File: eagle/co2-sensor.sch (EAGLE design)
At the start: 12 parts, among them IC1 LM1117IMPX-3.3, J1 MH-Z19, U1 esp12e, U2 dht22, X1 usb

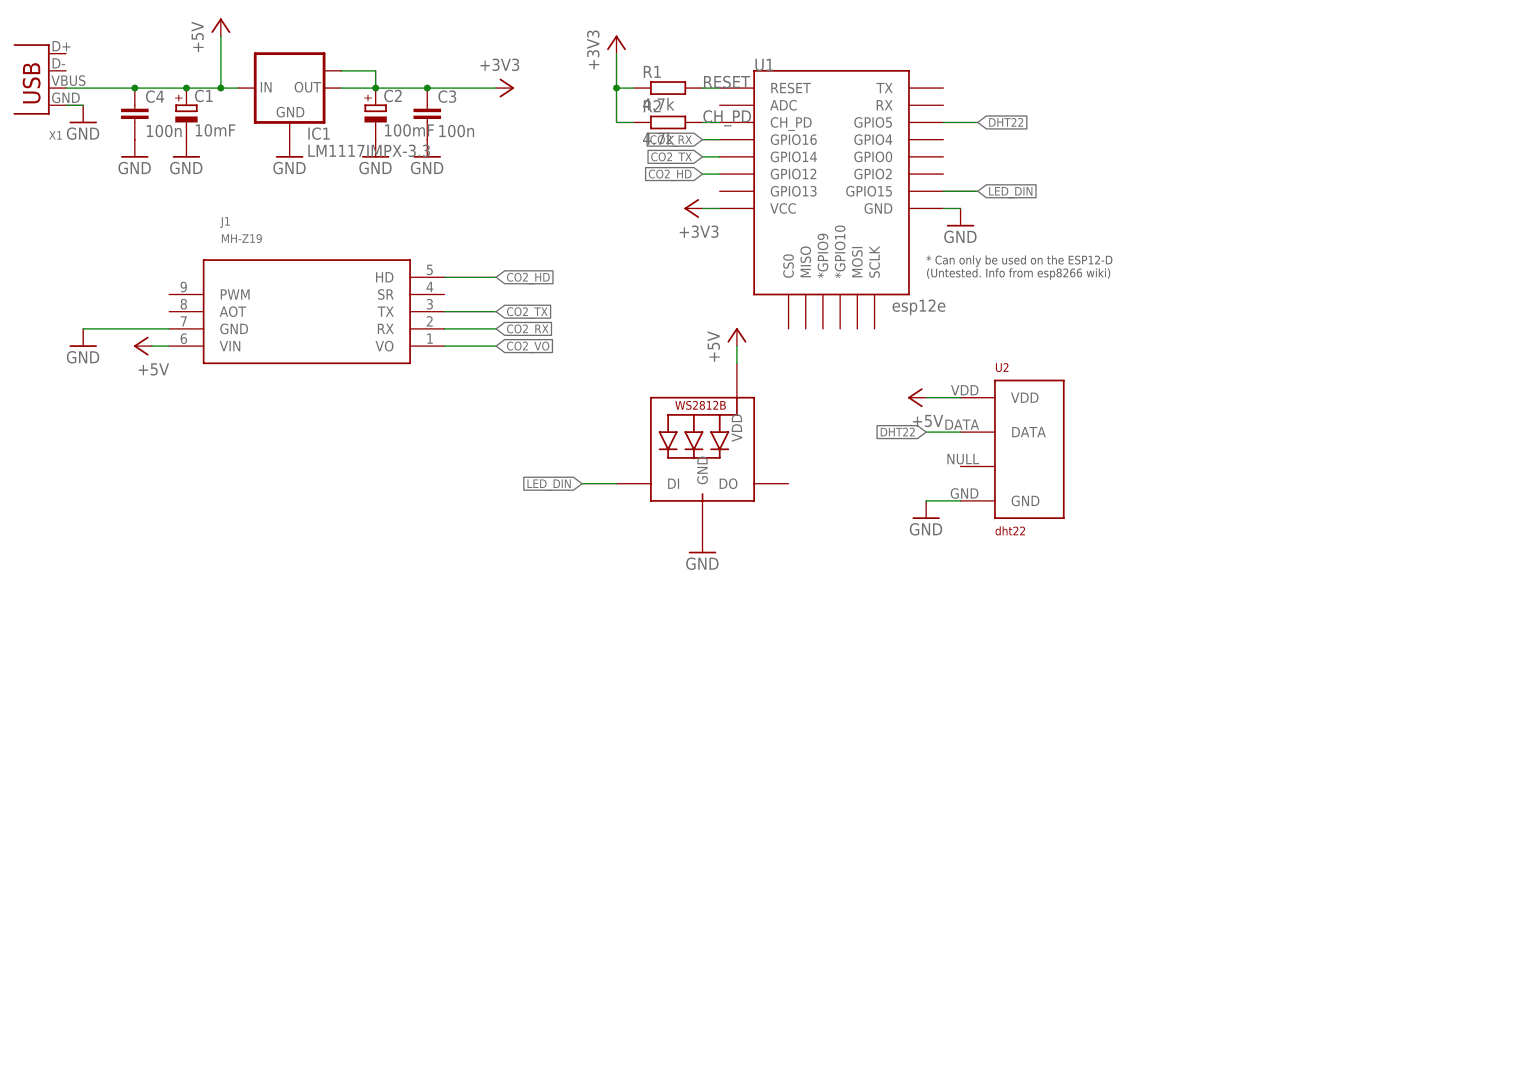
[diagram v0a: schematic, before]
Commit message: fixed prototype issues
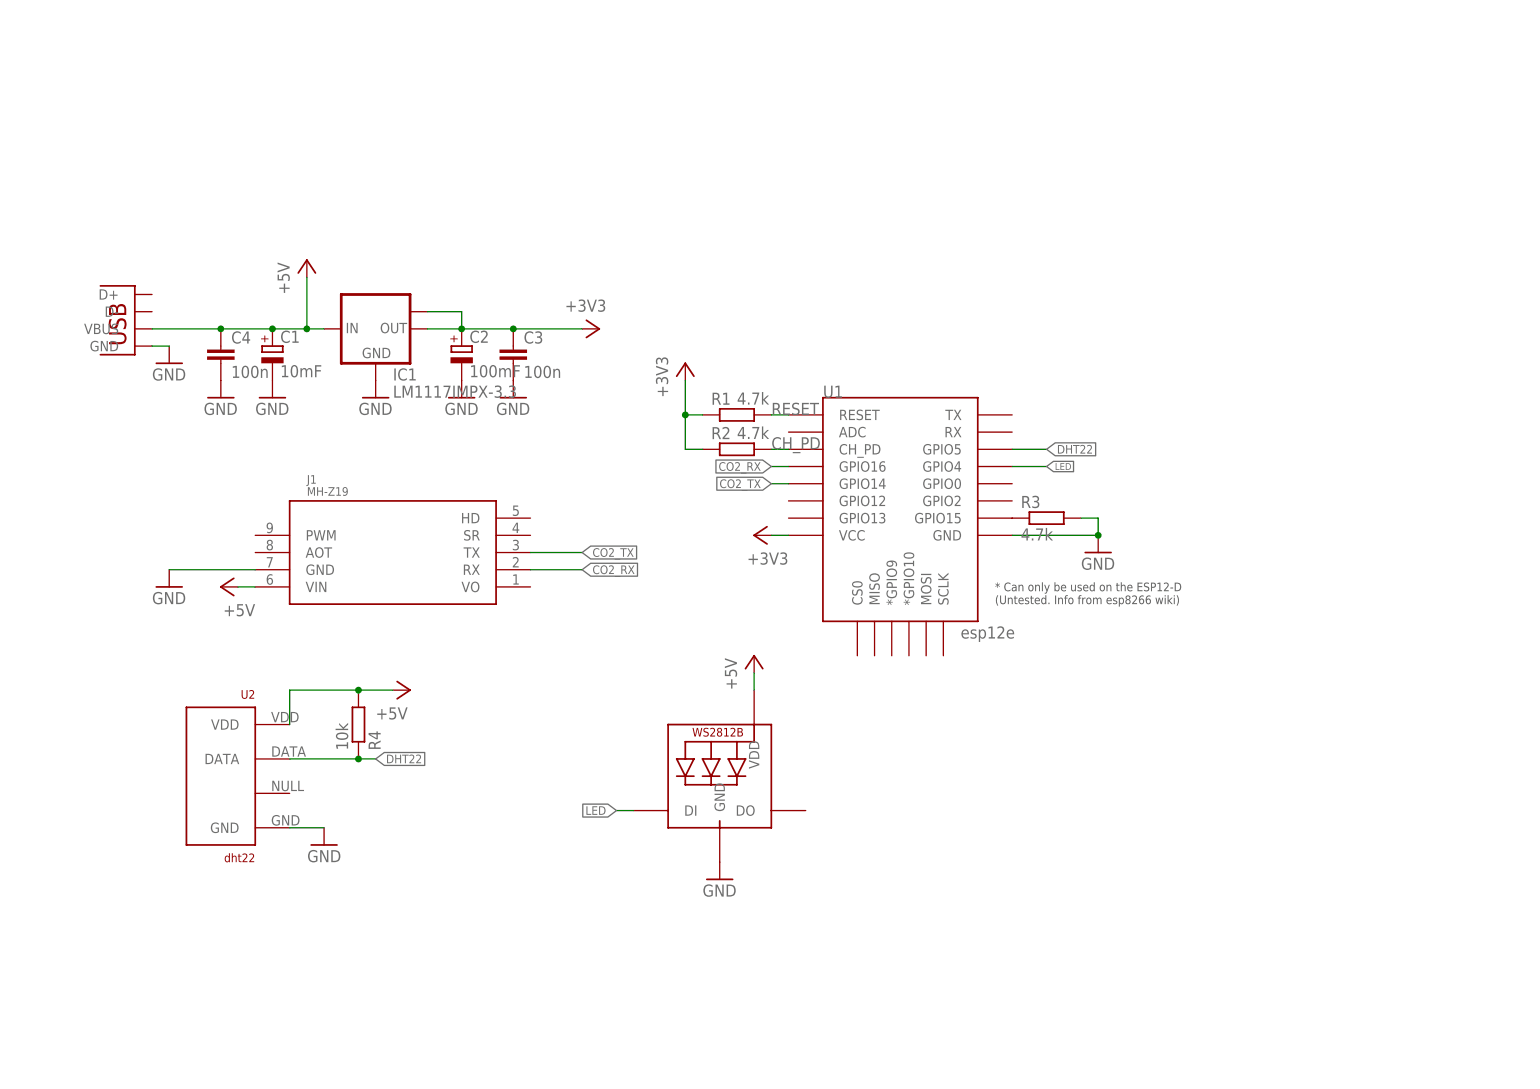
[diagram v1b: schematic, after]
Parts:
- removed X1: usb, con-usb-3:USB-A-H
- added R3: 4.7k, rcl:R-EU_M0805
- added R4: 10k, rcl:R-EU_M0805
- added U$1: USB-A, usb:USB-A
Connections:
- removed net CO2_HD: J1.HD, U1.GPIO12
- removed net CO2_VO: J1.VO
- removed net LED_DIN: LED1.DI, U1.GPIO15
- new net LED: LED1.DI, U1.GPIO4
- new net N$1: R3.1, U1.GPIO15
- net +5V: now also R4.2, U$1.VBUS; no longer X1.VBUS
- net DHT22: now also R4.1
- net GND: now also R3.2, U$1.GND@1; no longer X1.GND
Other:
- moved on the sheet: C1, C2, C3, C4, IC1, J1, R1, R2, U1, U2

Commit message: .
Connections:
- net GND: now also U$1.GND@2, U$1.GND@3
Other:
- moved on the sheet: R4

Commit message: .
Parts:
- removed C1: 10mF, rcl:CPOL-EUCT3216
- added BT1: BAT-HLD-012-SMT, BAT-HLD-012-SMT:BAT-HLD-012-SMT
- added IC2: (no value), DS3231_industrialberry:DS3231SOIC-16W
- added JP1: (no value), pinhead:PINHD-1X4
- added JP2: (no value), pinhead:PINHD-2X4
- added R5, R6: 4.7k, rcl:R-EU_M0805
- C4: value 100n -> 10u
- LED1: value WS2812B_5050N -> WS2812B5050; device WS2812B:WS2812B_5050N -> WS2812B:WS2812B5050
- U$1: value USB-A -> USB-C; device usb:USB-A -> USB-C:USB-C
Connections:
- removed net LED: LED1.DI, U1.GPIO4
- removed net RESET: R1.2, U1.RESET
- new net CLOCK_INT: IC2.!INT, U1.GPIO13
- new net IO0: JP2.5, U1.GPIO0
- new net IO2: JP2.3, LED1.DI, U1.GPIO2
- new net N$6: BT1.P, IC2.VBAT
- new net RST: IC2.!RST, JP2.6, R2.2, U1.RESET
- new net RXD: JP2.7, U1.RX
- new net SCL: IC2.SCL, JP1.3, R6.2, U1.GPIO5
- new net SDA: IC2.SDA, JP1.4, R5.2, U1.GPIO4
- new net TXD: JP2.2, U1.TX
- net +3V3: now also IC2.VCC, JP1.2, JP2.8, R5.1, R6.1
- net +5V: no longer C1.+
- net CH_PD: now also JP2.4, R1.2; no longer R2.2
- net DHT22: now also U1.GPIO12; no longer U1.GPIO5
- net GND: now also BT1.N, IC2.GND, IC2.NC@1, IC2.NC@2, IC2.NC@3, IC2.NC@4, IC2.NC@5, IC2.NC@6, IC2.NC@7, IC2.NC@8, JP1.1, JP2.1, U$1.GND; no longer C1.-, U$1.GND@1, U$1.GND@2, U$1.GND@3
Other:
- moved on the sheet: C4, R1, R2, R3, U1

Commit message: .
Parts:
- added C1: 100n, rcl:C-EUC0805
- added U3: BMP280, BMP280:BMP280
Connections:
- net +3V3: now also C1.1, U3.CSB, U3.VDD, U3.VDDIO
- net GND: now also C1.2, U3.GND, U3.SDO
- net SCL: now also U3.SCK
- net SDA: now also U3.SDI
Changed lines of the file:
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@@
 </variantdefs>
 <classes>
-<class number="0" name="default" width="0.2" drill="0">
+<class number="0" name="default" width="0.25" drill="0">
 <clearance class="0" value="0.205"/>
 </class>
-<class number="1" name="GND" width="1" drill="0">
+<class number="1" name="GND" width="0.8" drill="0">
 <clearance class="0" value="0.205"/>
 <clearance class="1" value="0.205"/>
 </class>
-<class number="2" name="+5V" width="0.8" drill="0">
+<class number="2" name="+5V" width="0.5" drill="0">
 <clearance class="0" value="0.205"/>
 <clearance class="1" value="0.205"/>
 <clearance class="2" value="0.205"/>
 </class>
-<class number="3" name="+3.3V" width="0.8" drill="0">
+<class number="3" name="+3.3V" width="0.5" drill="0">
 <clearance class="0" value="0.205"/>
 <clearance class="1" value="0.205"/>
@@
 <part name="GND12" library="supply1" library_urn="urn:adsk.eagle:library:371" deviceset="GND" device=""/>
 <part name="P+2" library="supply1" library_urn="urn:adsk.eagle:library:371" deviceset="+5V" device=""/>
+<part name="U3" library="BMP280" deviceset="BMP280" device=""/>
+<part name="GND13" library="supply1" library_urn="urn:adsk.eagle:library:371" deviceset="GND" device=""/>
+<part name="GND14" library="supply1" library_urn="urn:adsk.eagle:library:371" deviceset="GND" device=""/>
+<part name="+3V4" library="supply1" library_urn="urn:adsk.eagle:library:371" deviceset="+3V3" device=""/>
+<part name="C1" library="rcl" library_urn="urn:adsk.eagle:library:334" deviceset="C-EU" device="C0805" package3d_urn="urn:adsk.eagle:package:23617/2" value="100n"/>
+<part name="GND15" library="supply1" library_urn="urn:adsk.eagle:library:371" deviceset="GND" device=""/>
 </parts>
 <sheets>
@@
 <instance part="P+2" gate="1" x="187.96" y="-7.62" smashed="yes">
 <attribute name="VALUE" x="185.42" y="-12.7" size="1.778" layer="96" rot="R90"/>
+</instance>
+<instance part="U3" gate="G$1" x="35.56" y="-104.14" smashed="yes">
+<attribute name="NAME" x="25.3804" y="-96.50533125" size="1.78141875" layer="95"/>
+<attribute name="VALUE" x="25.3907" y="-114.3093" size="1.77963125" layer="96"/>
+</instance>
+<instance part="GND13" gate="1" x="48.26" y="-114.3" smashed="yes">
+<attribute name="VALUE" x="45.72" y="-116.84" size="1.778" layer="96"/>
+</instance>
+<instance part="GND14" gate="1" x="12.7" y="-114.3" smashed="yes">
+<attribute name="VALUE" x="10.16" y="-116.84" size="1.778" layer="96"/>
+</instance>
+<instance part="+3V4" gate="G$1" x="50.8" y="-91.44" smashed="yes">
+<attribute name="VALUE" x="48.26" y="-96.52" size="1.778" layer="96" rot="R90"/>
+</instance>
+<instance part="C1" gate="G$1" x="68.58" y="-10.16" smashed="yes">
+<attribute name="NAME" x="70.104" y="-9.779" size="1.778" layer="95"/>
+<attribute name="VALUE" x="70.104" y="-14.859" size="1.778" layer="96"/>
+</instance>
+<instance part="GND15" gate="1" x="68.58" y="-20.32" smashed="yes">
+<attribute name="VALUE" x="66.04" y="-22.86" size="1.778" layer="96"/>
 </instance>
 </instances>
@@
 <pinref part="GND12" gate="1" pin="GND"/>
 </segment>
+<segment>
+<pinref part="U3" gate="G$1" pin="GND"/>
+<pinref part="GND13" gate="1" pin="GND"/>
+<wire x1="48.26" y1="-109.22" x2="48.26" y2="-111.76" width="0.1524" layer="91"/>
+</segment>
+<segment>
+<pinref part="U3" gate="G$1" pin="SDO"/>
+<wire x1="22.86" y1="-104.14" x2="12.7" y2="-104.14" width="0.1524" layer="91"/>
+<wire x1="12.7" y1="-104.14" x2="12.7" y2="-111.76" width="0.1524" layer="91"/>
+<pinref part="GND14" gate="1" pin="GND"/>
+</segment>
+<segment>
+<pinref part="C1" gate="G$1" pin="2"/>
+<pinref part="GND15" gate="1" pin="GND"/>
+<wire x1="68.58" y1="-17.78" x2="68.58" y2="-15.24" width="0.1524" layer="91"/>
+</segment>
 </net>
 <net name="+3V3" class="3">
@@
 <pinref part="IC1" gate="G$1" pin="OUT1"/>
 <wire x1="53.34" y1="-7.62" x2="60.96" y2="-7.62" width="0.1524" layer="91"/>
-<wire x1="60.96" y1="-7.62" x2="71.12" y2="-7.62" width="0.1524" layer="91"/>
+<wire x1="60.96" y1="-7.62" x2="68.58" y2="-7.62" width="0.1524" layer="91"/>
+<wire x1="68.58" y1="-7.62" x2="71.12" y2="-7.62" width="0.1524" layer="91"/>
 <wire x1="48.26" y1="-5.08" x2="53.34" y2="-5.08" width="0.1524" layer="91"/>
 <wire x1="53.34" y1="-5.08" x2="53.34" y2="-7.62" width="0.1524" layer="91"/>
@@
 <pinref part="C3" gate="G$1" pin="1"/>
 <junction x="60.96" y="-7.62"/>
+<pinref part="C1" gate="G$1" pin="1"/>
+<junction x="68.58" y="-7.62"/>
 </segment>
 <segment>
@@
 <label x="144.78" y="-66.04" size="1.016" layer="95" rot="MR0" xref="yes"/>
 </segment>
+<segment>
+<pinref part="U3" gate="G$1" pin="CSB"/>
+<wire x1="22.86" y1="-99.06" x2="20.32" y2="-99.06" width="0.1524" layer="91"/>
+<wire x1="20.32" y1="-99.06" x2="20.32" y2="-93.98" width="0.1524" layer="91"/>
+<wire x1="20.32" y1="-93.98" x2="50.8" y2="-93.98" width="0.1524" layer="91"/>
+<wire x1="50.8" y1="-93.98" x2="50.8" y2="-99.06" width="0.1524" layer="91"/>
+<pinref part="U3" gate="G$1" pin="VDDIO"/>
+<wire x1="50.8" y1="-99.06" x2="50.8" y2="-101.6" width="0.1524" layer="91"/>
+<wire x1="50.8" y1="-101.6" x2="48.26" y2="-101.6" width="0.1524" layer="91"/>
+<pinref part="U3" gate="G$1" pin="VDD"/>
+<wire x1="48.26" y1="-99.06" x2="50.8" y2="-99.06" width="0.1524" layer="91"/>
+<junction x="50.8" y="-99.06"/>
+<pinref part="+3V4" gate="G$1" pin="+3V3"/>
+<junction x="50.8" y="-93.98"/>
+</segment>
 </net>
 <net name="+5V" class="2">
@@
 <label x="175.26" y="-63.5" size="1.016" layer="95" xref="yes"/>
 </segment>
+<segment>
+<pinref part="U3" gate="G$1" pin="SCK"/>
+<wire x1="22.86" y1="-106.68" x2="20.32" y2="-106.68" width="0.1524" layer="91"/>
+<label x="20.32" y="-106.68" size="1.016" layer="95" rot="MR0" xref="yes"/>
+</segment>
 </net>
 <net name="SDA" class="0">
@@
 <label x="175.26" y="-66.04" size="1.016" layer="95" xref="yes"/>
 </segment>
-</net>
+<segment>
+<pinref part="U3" gate="G$1" pin="SDI"/>
+<wire x1="22.86" y1="-101.6" x2="20.32" y2="-101.6" width="0.1524" layer="91"/>
+<label x="20.32" y="-101.6" size="1.016" layer="95" rot="MR0" xref="yes"/>
+</segment>
+</net>
